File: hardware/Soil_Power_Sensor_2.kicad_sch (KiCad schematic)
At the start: 12 parts, among them J8 Conn_01x10, U3 REF2033, U5 TPS60400DBV

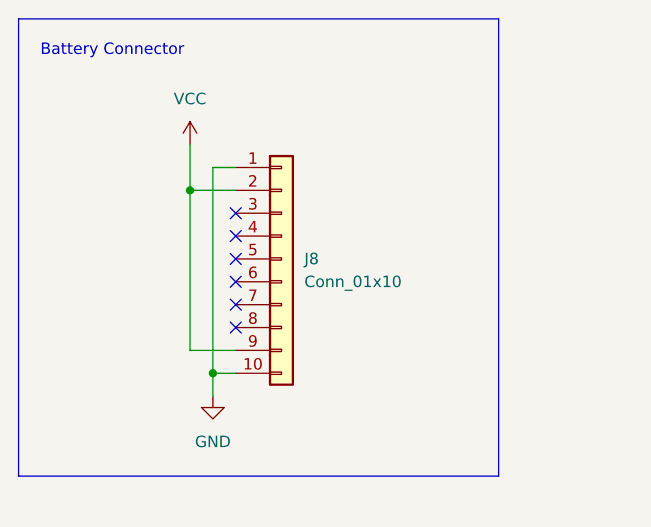
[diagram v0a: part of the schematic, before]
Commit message: Fixed issues from design review
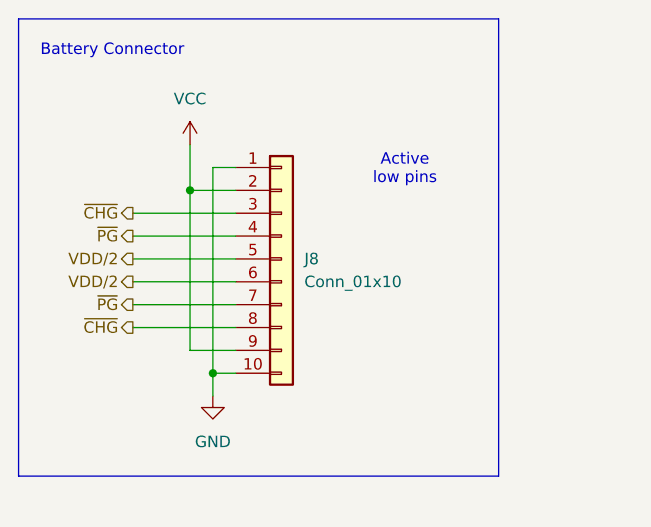
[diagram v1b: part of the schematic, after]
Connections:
- net ~{CHG}: now reaches J8.3 (Pin_3)
- net ~{CHG}: now also J8.8 (Pin_8)
- net ~{PG}: now reaches J8.4 (Pin_4)
- net ~{PG}: now also J8.7 (Pin_7)
- net VDD/2: now reaches J8.5 (Pin_5)
- net VDD/2: now also J8.6 (Pin_6)
- no-connect marks 6 -> 0
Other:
- note added: "Active low pins"
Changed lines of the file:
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@@
 		(color 0 0 0 0)
 	)
-	(no_connect
-		(at 43.18 46.99)
-	)
-	(no_connect
-		(at 43.18 39.37)
-	)
-	(no_connect
-		(at 43.18 49.53)
-	)
-	(no_connect
-		(at 43.18 52.07)
-	)
-	(no_connect
-		(at 43.18 44.45)
-	)
-	(no_connect
-		(at 43.18 41.91)
-	)
 	(wire
 		(pts
@@
 	(wire
 		(pts
+			(xy 31.75 44.45) (xy 43.18 44.45)
+		)
+		(stroke
+			(width 0)
+			(type default)
+		)
+	)
+	(wire
+		(pts
 			(xy 90.17 124.46) (xy 90.17 137.16)
 		)
@@
 	(wire
 		(pts
+			(xy 31.75 49.53) (xy 43.18 49.53)
+		)
+		(stroke
+			(width 0)
+			(type default)
+		)
+	)
+	(wire
+		(pts
 			(xy 54.61 146.05) (xy 54.61 144.78)
 		)
@@
 	(wire
 		(pts
+			(xy 31.75 52.07) (xy 43.18 52.07)
+		)
+		(stroke
+			(width 0)
+			(type default)
+		)
+	)
+	(wire
+		(pts
 			(xy 83.82 154.94) (xy 83.82 149.86)
 		)
@@
 	(wire
 		(pts
+			(xy 31.75 39.37) (xy 43.18 39.37)
+		)
+		(stroke
+			(width 0)
+			(type default)
+		)
+	)
+	(wire
+		(pts
 			(xy 181.61 45.72) (xy 181.61 50.8)
 		)
@@
 	(wire
 		(pts
+			(xy 31.75 46.99) (xy 43.18 46.99)
+		)
+		(stroke
+			(width 0)
+			(type default)
+		)
+	)
+	(wire
+		(pts
 			(xy 242.57 50.8) (xy 242.57 53.34)
 		)
@@
 			(width 0.1524)
 			(type solid)
+		)
+	)
+	(wire
+		(pts
+			(xy 31.75 41.91) (xy 43.18 41.91)
+		)
+		(stroke
+			(width 0)
+			(type default)
 		)
 	)
@@
 		(fill
 			(type none)
+		)
+	)
+	(text "Active\nlow pins"
+		(exclude_from_sim no)
+		(at 61.976 34.544 0)
+		(effects
+			(font
+				(size 1.27 1.27)
+			)
 		)
 	)
@@
 		)
 	)
+	(hierarchical_label "~{CHG}"
+		(shape output)
+		(at 31.75 52.07 180)
+		(fields_autoplaced yes)
+		(effects
+			(font
+				(size 1.27 1.27)
+			)
+			(justify right)
+		)
+	)
+	(hierarchical_label "~{PG}"
+		(shape output)
+		(at 31.75 49.53 180)
+		(fields_autoplaced yes)
+		(effects
+			(font
+				(size 1.27 1.27)
+			)
+			(justify right)
+		)
+	)
+	(hierarchical_label "VDD{slash}2"
+		(shape output)
+		(at 31.75 44.45 180)
+		(fields_autoplaced yes)
+		(effects
+			(font
+				(size 1.27 1.27)
+			)
+			(justify right)
+		)
+	)
+	(hierarchical_label "~{CHG}"
+		(shape output)
+		(at 31.75 39.37 180)
+		(fields_autoplaced yes)
+		(effects
+			(font
+				(size 1.27 1.27)
+			)
+			(justify right)
+		)
+	)
+	(hierarchical_label "~{PG}"
+		(shape output)
+		(at 31.75 41.91 180)
+		(fields_autoplaced yes)
+		(effects
+			(font
+				(size 1.27 1.27)
+			)
+			(justify right)
+		)
+	)
 	(hierarchical_label "POWERDOWN"
 		(shape input)
@@
 		(fields_autoplaced yes)
 		(effects
+			(font
+				(size 1.27 1.27)
+			)
+			(justify right)
+		)
+	)
+	(hierarchical_label "VDD{slash}2"
+		(shape output)
+		(at 31.75 46.99 180)
+		(fields_autoplaced yes)
+		(effects

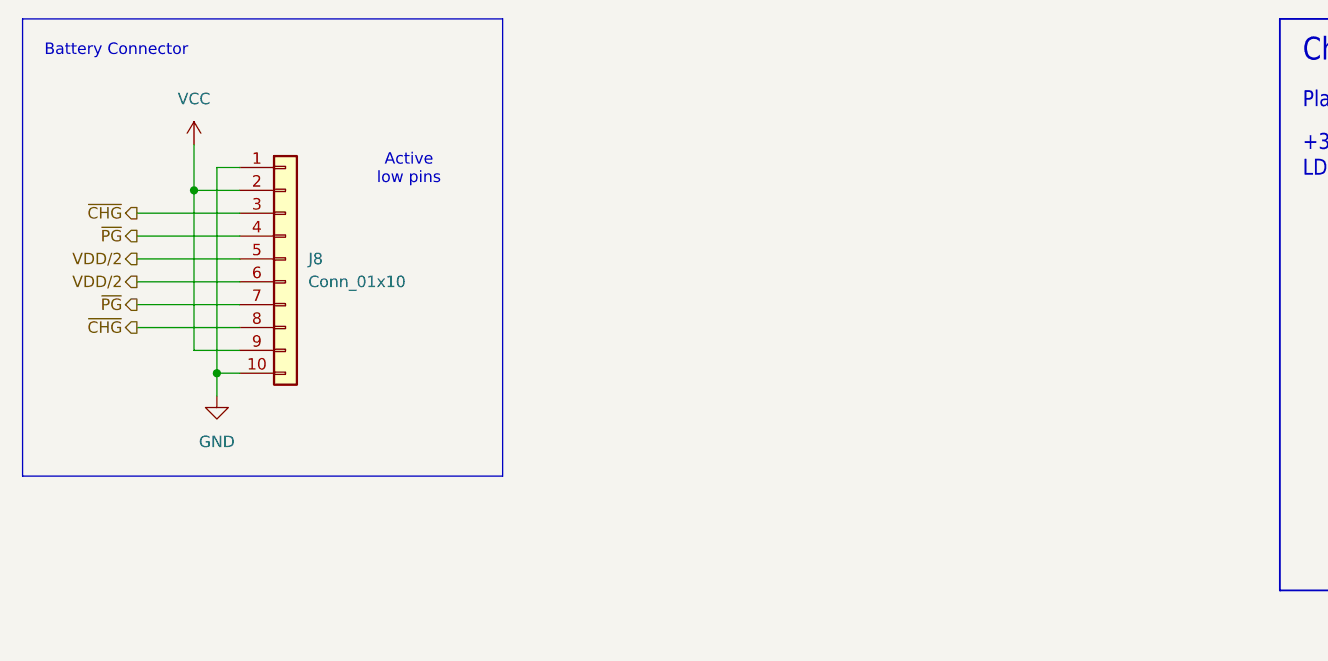
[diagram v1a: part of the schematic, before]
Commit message: Fixed issue with battery connector
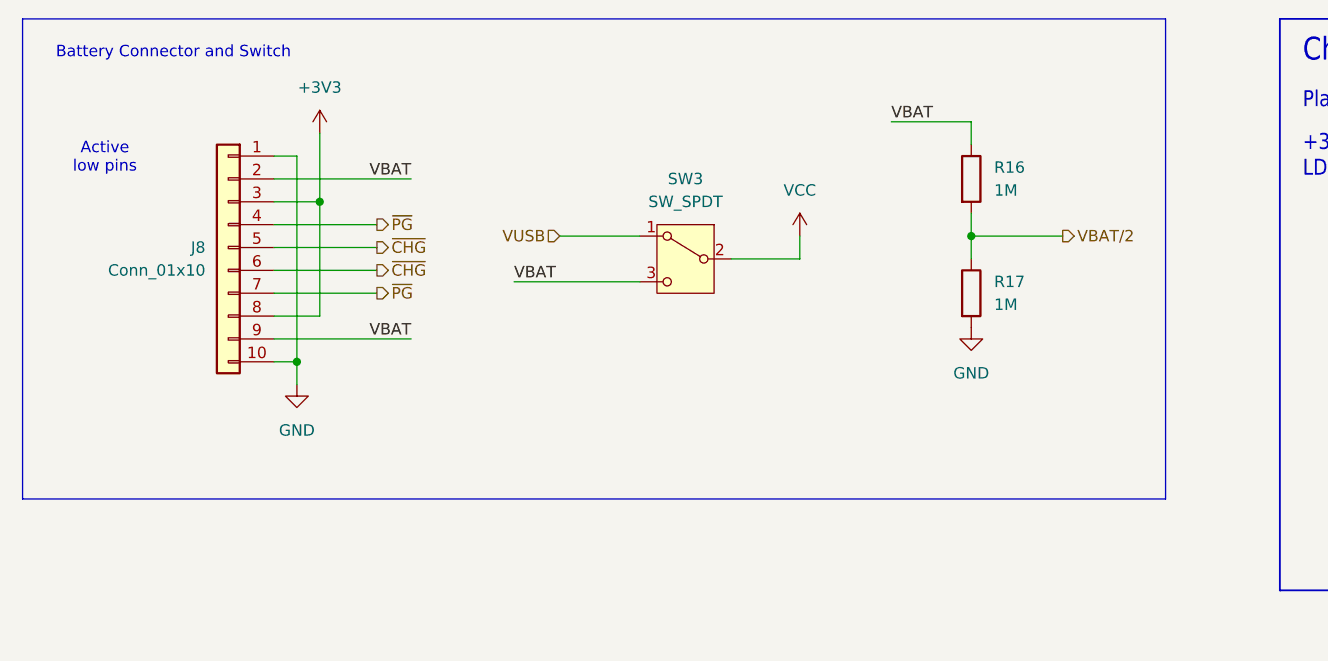
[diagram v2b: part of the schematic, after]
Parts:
- added R16, R17: 1M, Resistor_SMD:R_0603_1608Metric, symbol Device:R
- added SW3: SW_SPDT, Soil Power Sensor:JS102011SCQN, symbol Switch:SW_SPDT
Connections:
- net VDD/2 is gone; now on net ~{CHG}: J8.5 (Pin_5), J8.6 (Pin_6)
- net +3V3: now also J8.3 (Pin_3), J8.8 (Pin_8)
- net GND: now also R17.2
- net VCC: now also SW3.2 (B); no longer J8.2 (Pin_2), J8.9 (Pin_9)
- net ~{CHG}: no longer J8.3 (Pin_3), J8.8 (Pin_8)
- new net VBAT: J8.2 (Pin_2), J8.9 (Pin_9), R16.1, SW3.3 (C)
- new net VBAT/2: R16.2, R17.1
- new net VUSB: SW3.1 (A)
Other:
- note added: "Battery Connector and Switch"
- note removed: "Battery Connector"
- moved on the sheet: J8

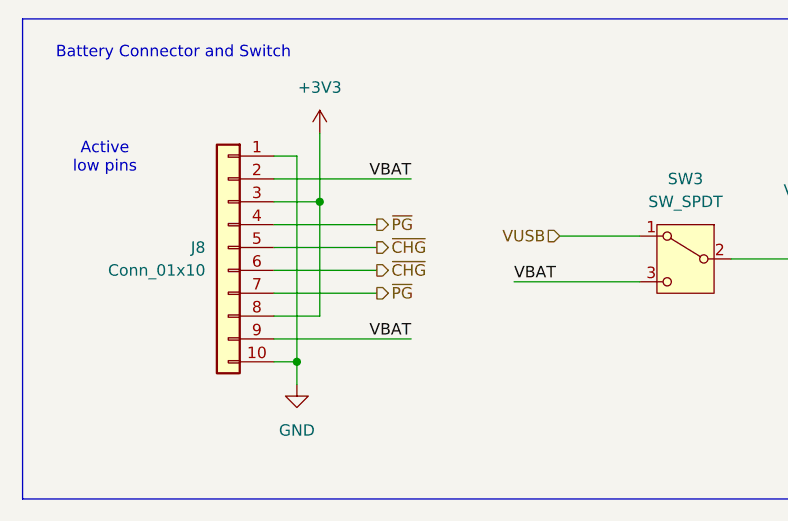
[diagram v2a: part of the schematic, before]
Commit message: Updated battery header
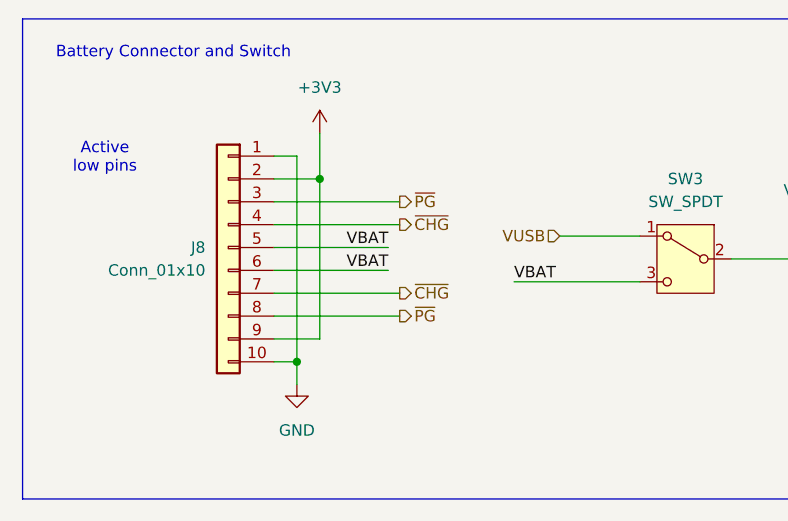
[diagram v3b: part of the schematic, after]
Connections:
- net +3V3: now also J8.2 (Pin_2), J8.9 (Pin_9); no longer J8.3 (Pin_3), J8.8 (Pin_8)
- net VBAT: now also J8.5 (Pin_5), J8.6 (Pin_6); no longer J8.2 (Pin_2), J8.9 (Pin_9)
- net ~{CHG}: now also J8.4 (Pin_4), J8.7 (Pin_7); no longer J8.5 (Pin_5), J8.6 (Pin_6)
- net ~{PG}: now also J8.3 (Pin_3), J8.8 (Pin_8); no longer J8.4 (Pin_4), J8.7 (Pin_7)
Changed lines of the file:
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@@
 	(title_block
 		(title "Soil Power Sensor")
-		(date "2024-11-14")
+		(date "2024-12-07")
 		(rev "2.2.3")
 		(company "jlab")
@@
 	)
 	(junction
+		(at 52.07 35.56)
+		(diameter 0)
+		(color 0 0 0 0)
+	)
+	(junction
 		(at 181.61 50.8)
 		(diameter 0)
@@
 	)
 	(junction
-		(at 52.07 38.1)
-		(diameter 0)
-		(color 0 0 0 0)
-	)
-	(junction
 		(at 242.57 50.8)
 		(diameter 0)
@@
 	(wire
 		(pts
-			(xy 46.99 35.56) (xy 62.23 35.56)
+			(xy 46.99 43.18) (xy 59.69 43.18)
 		)
 		(stroke
@@
 	(wire
 		(pts
+			(xy 46.99 40.64) (xy 60.96 40.64)
+		)
+		(stroke
+			(width 0)
+			(type default)
+		)
+	)
+	(wire
+		(pts
 			(xy 54.61 127) (xy 54.61 128.27)
 		)
@@
 	(wire
 		(pts
-			(xy 46.99 53.34) (xy 62.23 53.34)
+			(xy 46.99 45.72) (xy 59.69 45.72)
 		)
 		(stroke
@@
 	(wire
 		(pts
-			(xy 58.42 43.18) (xy 46.99 43.18)
-		)
-		(stroke
-			(width 0)
-			(type default)
-		)
-	)
-	(wire
-		(pts
 			(xy 124.46 41.91) (xy 134.62 41.91)
 		)
@@
 	(wire
 		(pts
-			(xy 58.42 48.26) (xy 46.99 48.26)
-		)
-		(stroke
-			(width 0)
-			(type default)
-		)
-	)
-	(wire
-		(pts
 			(xy 54.61 146.05) (xy 54.61 144.78)
 		)
@@
 	(wire
 		(pts
-			(xy 52.07 38.1) (xy 46.99 38.1)
+			(xy 52.07 35.56) (xy 46.99 35.56)
 		)
 		(stroke
@@
 	(wire
 		(pts
-			(xy 52.07 30.48) (xy 52.07 38.1)
+			(xy 52.07 30.48) (xy 52.07 35.56)
 		)
 		(stroke
@@
 	(wire
 		(pts
+			(xy 52.07 35.56) (xy 52.07 53.34)
+		)
+		(stroke
+			(width 0)
+			(type default)
+		)
+	)
+	(wire
+		(pts
 			(xy 71.12 139.7) (xy 95.25 139.7)
 		)
@@
 	(wire
 		(pts
-			(xy 52.07 38.1) (xy 52.07 50.8)
-		)
-		(stroke
-			(width 0)
-			(type default)
-		)
-	)
-	(wire
-		(pts
 			(xy 71.12 139.7) (xy 71.12 142.24)
 		)
@@
 	(wire
 		(pts
+			(xy 46.99 48.26) (xy 60.96 48.26)
+		)
+		(stroke
+			(width 0)
+			(type default)
+		)
+	)
+	(wire
+		(pts
 			(xy 124.46 29.21) (xy 124.46 31.75)
 		)
@@
 	(wire
 		(pts
-			(xy 52.07 50.8) (xy 46.99 50.8)
+			(xy 52.07 53.34) (xy 46.99 53.34)
 		)
 		(stroke
@@
 	(wire
 		(pts
-			(xy 58.42 45.72) (xy 46.99 45.72)
-		)
-		(stroke
-			(width 0)
-			(type default)
-		)
-	)
-	(wire
-		(pts
 			(xy 242.57 50.8) (xy 242.57 53.34)
 		)
@@
 	(wire
 		(pts
-			(xy 58.42 40.64) (xy 46.99 40.64)
+			(xy 46.99 38.1) (xy 60.96 38.1)
 		)
 		(stroke
@@
 			(width 0.1524)
 			(type solid)
+		)
+	)
+	(wire
+		(pts
+			(xy 46.99 50.8) (xy 60.96 50.8)
+		)
+		(stroke
+			(width 0)
+			(type default)
 		)
 	)
@@
 	)
 	(label "VBAT"
-		(at 62.23 53.34 180)
+		(at 59.69 45.72 180)
 		(fields_autoplaced yes)
 		(effects
@@
 	)
 	(label "VBAT"
-		(at 62.23 35.56 180)
+		(at 59.69 43.18 180)
 		(fields_autoplaced yes)
 		(effects
@@
 	(hierarchical_label "~{CHG}"
 		(shape output)
-		(at 58.42 45.72 0)
+		(at 60.96 48.26 0)
 		(fields_autoplaced yes)
 		(effects
@@
 	(hierarchical_label "~{PG}"
 		(shape output)
-		(at 58.42 48.26 0)
+		(at 60.96 50.8 0)
 		(fields_autoplaced yes)
 		(effects
@@
 	(hierarchical_label "~{CHG}"
 		(shape output)
-		(at 58.42 43.18 0)
+		(at 60.96 40.64 0)
 		(fields_autoplaced yes)
 		(effects
@@
 	(hierarchical_label "~{PG}"
 		(shape output)
-		(at 58.42 40.64 0)
-		(fields_autoplaced yes)
-		(effects
+		(at 60.96 38.1 0)
+		(fields_autoplaced yes)
+		(effects

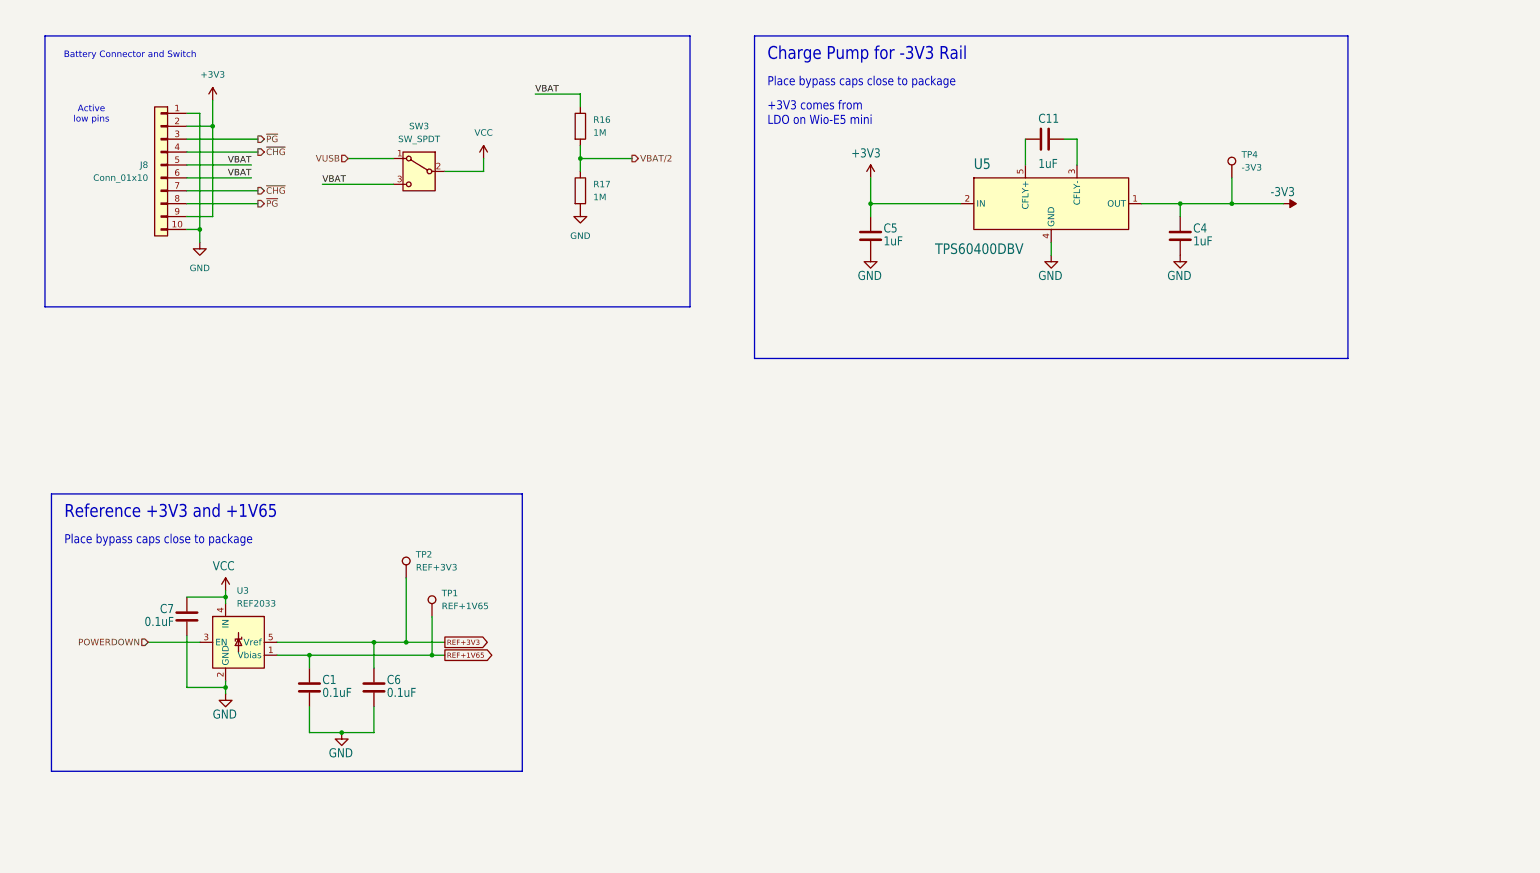
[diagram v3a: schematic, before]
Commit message: replace mini with module
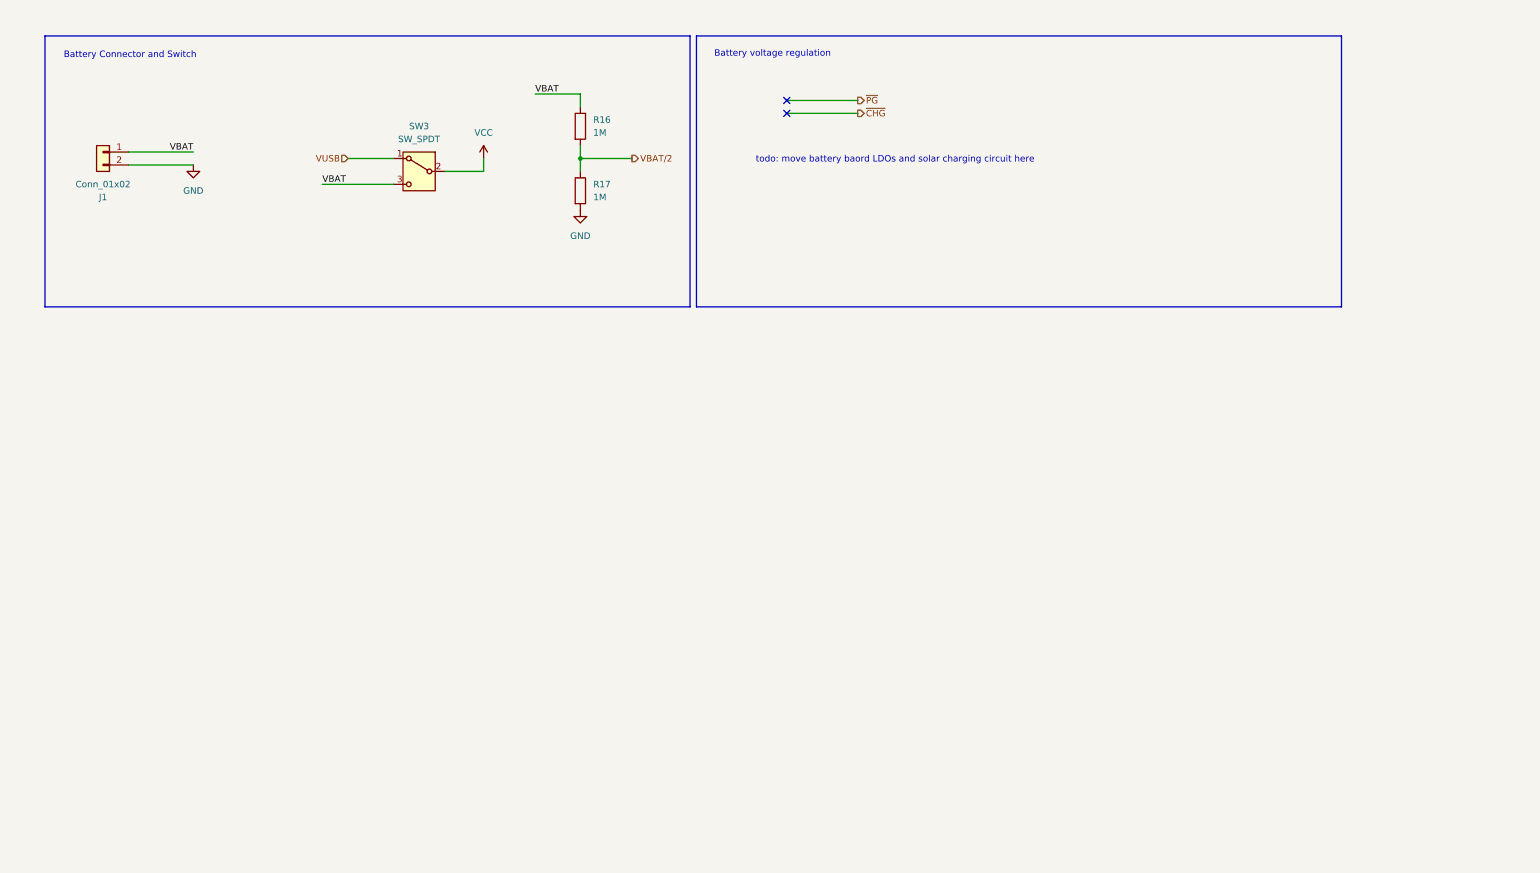
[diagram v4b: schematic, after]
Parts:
- removed C1, C6, C7: 0.1uF, Capacitor_SMD:C_0603_1608Metric, symbol Device:C
- removed C11, C4, C5: 1uF, Capacitor_SMD:C_0603_1608Metric, symbol Device:C
- removed J8: Conn_01x10, Connector_PinHeader_2.54mm:PinHeader_1x10_P2.54mm_Horizontal, symbol Connector_Generic:Conn_01x10
- removed TP1: REF+1V65, TestPoint:TestPoint_Pad_D1.5mm, symbol Connector:TestPoint
- removed TP2: REF+3V3, TestPoint:TestPoint_Pad_D1.5mm, symbol Connector:TestPoint
- removed TP4: -3V3, TestPoint:TestPoint_Pad_D1.5mm, symbol Connector:TestPoint
- removed U3: REF2033, Package_TO_SOT_SMD:SOT-23-5, symbol Reference_Voltage:REF2033
- removed U5: TPS60400DBV, Package_TO_SOT_SMD:SOT-23-5, symbol Soil Power Sensor-eagle-import:TPS60400DBV
- added J1: Conn_01x02, Connector_JST:JST_PH_S2B-PH-K_1x02_P2.00mm_Horizontal, symbol Connector_Generic:Conn_01x02
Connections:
- net GND: now also J1.2 (Pin_2)
- net VBAT: now also J1.1 (Pin_1)
- no-connect marks 0 -> 2
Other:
- note added: "Battery voltage regulation"
- note added: "todo: move battery baord LDOs and solar charging circuit here"
- note removed: "+3V3 comes from LDO on Wio-E5 mini"
- note removed: "Active low pins"
- note removed: "Charge Pump for -3V3 Rail"
- note removed: "Place bypass caps close to package"
- note removed: "Reference +3V3 and +1V65"
